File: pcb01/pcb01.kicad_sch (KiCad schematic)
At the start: 51 parts, among them J1 DIN41612_02x32_AC, J10 Conn_01x02_Socket, J11 Conn_01x09, J4 Display, J5 UART, J6 UART_IRQ, J7 Jmp_Irq, J8 Jmp_NMI, J9 Ram1 Enable, SW1 SW_Push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

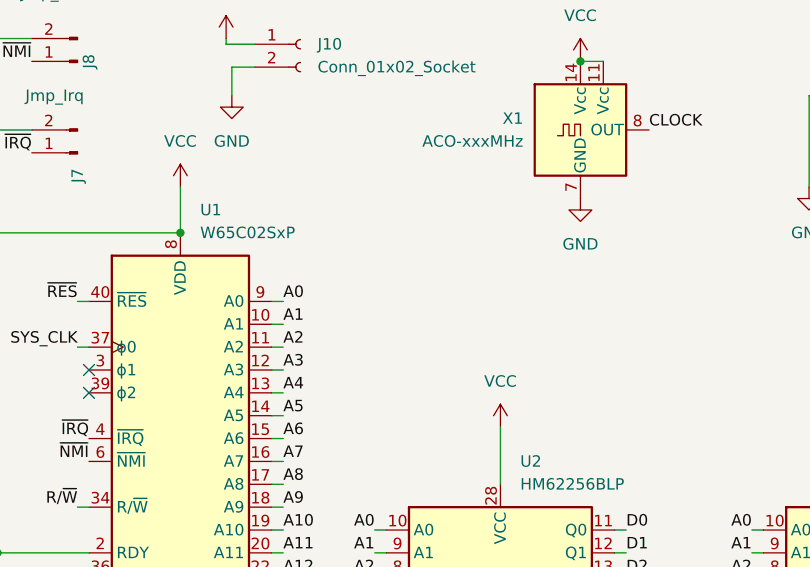
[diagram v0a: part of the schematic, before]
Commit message: fixed errors of first pcb (hopefully didn't mess up everything)
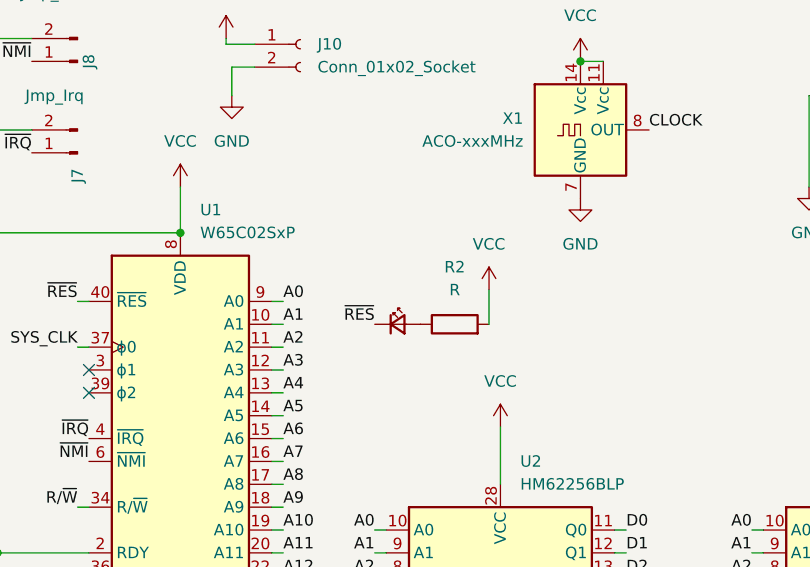
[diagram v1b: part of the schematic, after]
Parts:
- added D13: LED_Small, LED_SMD:LED_0805_2012Metric_Pad1.15x1.40mm_HandSolder, symbol Device:LED_Small
- added R2: R, Resistor_THT:R_Axial_DIN0207_L6.3mm_D2.5mm_P7.62mm_Horizontal, symbol Device:R
- C12, C13: footprint Capacitor_THT:CP_Radial_D5.0mm_P2.50mm -> Capacitor_THT:CP_Radial_D4.0mm_P2.00mm
- J6, J7, J8: footprint Connector_PinHeader_2.00mm:PinHeader_1x02_P2.00mm_Vertical -> Connector_PinSocket_2.54mm:PinSocket_1x02_P2.54mm_Vertical
- RN1, RN2, RN3: footprint Resistor_SMD:R_Array_Concave_4x0402 -> Resistor_SMD:R_Array_Convex_4x0612
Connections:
- net VCC: now also R2.2
- net ~{RES}: now also D13.1 (K)
- new net: D13.2 (A), R2.1
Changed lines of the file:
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@@
     (stroke (width 0) (type default))
   )
+  (wire (pts (xy 74.93 46.99) (xy 74.93 50.8))
+    (stroke (width 0) (type default))
+  )
   (wire (pts (xy 208.28 55.88) (xy 208.28 62.23))
     (stroke (width 0) (type default))
@@
     (effects (font (size 1.27 1.27)) (justify right bottom))
   )
+  (label "~{RES}" (at 62.23 50.8 180) (fields_autoplaced)
+    (effects (font (size 1.27 1.27)) (justify right bottom))
+  )
   (label "D3" (at 132.08 81.28 0) (fields_autoplaced)
     (effects (font (size 1.27 1.27)) (justify left bottom))
@@
       (effects (font (size 1.27 1.27)))
     )
-    (property "Footprint" "Connector_PinHeader_2.00mm:PinHeader_1x02_P2.00mm_Vertical" (at 29.21 31.75 0)
+    (property "Footprint" "Connector_PinSocket_2.54mm:PinSocket_1x02_P2.54mm_Vertical" (at 29.21 31.75 0)
       (effects (font (size 1.27 1.27)) hide)
     )
@@
     )
   )
+  (symbol (lib_id "Device:R") (at 71.12 50.8 90) (unit 1)
+    (in_bom yes) (on_board yes) (dnp no) (fields_autoplaced)
+    (property "Reference" "R2" (at 71.12 44.45 90)
+      (effects (font (size 1.27 1.27)))
+    )
+    (property "Value" "R" (at 71.12 46.99 90)
+      (effects (font (size 1.27 1.27)))
+    )
+    (property "Footprint" "Resistor_THT:R_Axial_DIN0207_L6.3mm_D2.5mm_P7.62mm_Horizontal" (at 71.12 52.578 90)
+      (effects (font (size 1.27 1.27)) hide)
+    )
+    (property "Datasheet" "~" (at 71.12 50.8 0)
+      (effects (font (size 1.27 1.27)) hide)
+    )
+    (pin "1")
+    (pin "2")
+    (instances
+      (project "pcb01"
+        (path "/a9a73dc6-7f92-4458-9da8-49621d12e480"
+          (reference "R2") (unit 1)
+        )
+      )
+    )
+  )
   (symbol (lib_id "Device:LED_Small") (at 279.4 143.51 0) (unit 1)
     (in_bom yes) (on_board yes) (dnp no)
@@
       (effects (font (size 1.27 1.27)))
     )
-    (property "Footprint" "Connector_PinHeader_2.00mm:PinHeader_1x02_P2.00mm_Vertical" (at 189.23 86.36 0)
+    (property "Footprint" "Connector_PinSocket_2.54mm:PinSocket_1x02_P2.54mm_Vertical" (at 189.23 86.36 0)
       (effects (font (size 1.27 1.27)) hide)
     )
@@
       (effects (font (size 1.27 1.27)))
     )
-    (property "Footprint" "Connector_PinHeader_2.00mm:PinHeader_1x02_P2.00mm_Vertical" (at 29.21 21.59 0)
+    (property "Footprint" "Connector_PinSocket_2.54mm:PinSocket_1x02_P2.54mm_Vertical" (at 29.21 21.59 0)
       (effects (font (size 1.27 1.27)) hide)
     )
@@
       (effects (font (size 1.27 1.27)) hide)
     )
-    (property "Footprint" "Resistor_SMD:R_Array_Concave_4x0402" (at 267.97 92.075 90)
+    (property "Footprint" "Resistor_SMD:R_Array_Convex_4x0612" (at 267.97 92.075 90)
       (effects (font (size 1.27 1.27)) hide)
     )
@@
       (effects (font (size 1.27 1.27)) (justify left))
     )
-    (property "Footprint" "Capacitor_THT:CP_Radial_D5.0mm_P2.50mm" (at 260.6802 24.765 0)
+    (property "Footprint" "Capacitor_THT:CP_Radial_D4.0mm_P2.00mm" (at 260.6802 24.765 0)
       (effects (font (size 1.27 1.27)) hide)
     )
@@
       (effects (font (size 1.27 1.27)) hide)
     )
-    (property "Footprint" "Resistor_SMD:R_Array_Concave_4x0402" (at 271.78 131.445 90)
+    (property "Footprint" "Resistor_SMD:R_Array_Convex_4x0612" (at 271.78 131.445 90)
       (effects (font (size 1.27 1.27)) hide)
     )
@@
     )
   )
+  (symbol (lib_id "power:VCC") (at 74.93 46.99 0) (unit 1)
+    (in_bom yes) (on_board yes) (dnp no) (fields_autoplaced)
+    (property "Reference" "#PWR037" (at 74.93 50.8 0)
+      (effects (font (size 1.27 1.27)) hide)
+    )
+    (property "Value" "VCC" (at 74.93 41.91 0)
+      (effects (font (size 1.27 1.27)))
+    )
+    (property "Footprint" "" (at 74.93 46.99 0)
+      (effects (font (size 1.27 1.27)) hide)
+    )
+    (property "Datasheet" "" (at 74.93 46.99 0)
+      (effects (font (size 1.27 1.27)) hide)
+    )
+    (pin "1")
+    (instances
+      (project "pcb01"
+        (path "/a9a73dc6-7f92-4458-9da8-49621d12e480"
+          (reference "#PWR037") (unit 1)
+        )
+      )
+    )
+  )
   (symbol (lib_id "Connector:Conn_01x02_Socket") (at 53.975 19.685 0) (unit 1)
     (in_bom yes) (on_board yes) (dnp no) (fields_autoplaced)
@@
       (effects (font (size 1.27 1.27)) (justify left))
     )
-    (property "Footprint" "Capacitor_THT:CP_Radial_D5.0mm_P2.50mm" (at 254.9652 24.765 0)
+    (property "Footprint" "Capacitor_THT:CP_Radial_D4.0mm_P2.00mm" (at 254.9652 24.765 0)
       (effects (font (size 1.27 1.27)) hide)
     )
@@
       (effects (font (size 1.27 1.27)) hide)
     )
-    (property "Footprint" "Resistor_SMD:R_Array_Concave_4x0402" (at 267.97 80.645 90)
+    (property "Footprint" "Resistor_SMD:R_Array_Convex_4x0612" (at 267.97 80.645 90)
       (effects (font (size 1.27 1.27)) hide)
     )
@@
         )
       )
+    )
+  )
+  (symbol (lib_id "Device:LED_Small") (at 64.77 50.8 0) (unit 1)
+    (in_bom yes) (on_board yes) (dnp no)
+    (property "Reference" "D13" (at 69.85 50.8 0)
+      (effects (font (size 1.27 1.27)) hide)
+    )
+    (property "Value" "LED_Small" (at 64.8335 46.99 0)
+      (effects (font (size 1.27 1.27)) hide)
+    )
+    (property "Footprint" "LED_SMD:LED_0805_2012Metric_Pad1.15x1.40mm_HandSolder" (at 64.77 50.8 90)
+      (effects (font (size 1.27 1.27)) hide)
+    )
+    (property "Datasheet" "~" (at 64.77 50.8 90)
+      (effects (font (size 1.27 1.27)) hide)
+    )
+    (pin "1")
+    (pin "2")
+    (instances
+      (project "pcb01"
+        (path "/a9a73dc6-7f92-4458-9da8-49621d12e480"
+          (reference "D13") (unit 1)
+        )
+      )

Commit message: big chunk of new pcb done
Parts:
- removed J4: Display, Connector_PinSocket_2.54mm:PinSocket_1x16_P2.54mm_Vertical, symbol Connector:Conn_01x16_Socket
- removed J6: UART_IRQ, Connector_PinSocket_2.54mm:PinSocket_1x02_P2.54mm_Vertical, symbol Connector:Conn_01x02_Socket
- removed RV1: R_LCD_BIAS, Potentiometer_THT:Potentiometer_Vishay_T73YP_Vertical, symbol Device:R_Potentiometer_Small
- removed U8: R565c52, Package_DIP:DIP-40_W15.24mm_Socket, symbol 65xx:R565c52
- added C14: C, Capacitor_THT:C_Disc_D4.7mm_W2.5mm_P5.00mm, symbol Device:C
- added U10: TL28L92FR, Package_QFP:MQFP-44_10x10mm_P0.8mm, symbol 2024-09-25_17-04-06:TL28L92FR
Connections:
- net A0: now also J1.a17 (Pin_a17), U10.40 (A0); no longer J1.c31 (Pin_c31)
- net A1: now also J1.a16 (Pin_a16), U10.42 (A1); no longer J1.c30 (Pin_c30)
- net A10: now also J1.a7 (Pin_a7); no longer J1.c21 (Pin_c21)
- net A11: now also J1.a6 (Pin_a6); no longer J1.c20 (Pin_c20)
- net A12: now also J1.a5 (Pin_a5); no longer J1.c19 (Pin_c19)
- net A13: now also J1.a4 (Pin_a4); no longer J1.c18 (Pin_c18)
- net A14: now also J1.a3 (Pin_a3); no longer J1.c17 (Pin_c17)
- net A15: now also J1.a2 (Pin_a2); no longer J1.c16 (Pin_c16)
- net A2: now also J1.a15 (Pin_a15), U10.44 (A2); no longer J1.c29 (Pin_c29)
- net A3: now also J1.a14 (Pin_a14), U10.1 (A3); no longer J1.c28 (Pin_c28)
- net A4: now also J1.a13 (Pin_a13); no longer J1.c27 (Pin_c27)
- net A5: now also J1.a12 (Pin_a12); no longer J1.c26 (Pin_c26)
- net A6: now also J1.a11 (Pin_a11); no longer J1.c25 (Pin_c25)
- net A7: now also J1.a10 (Pin_a10); no longer J1.c24 (Pin_c24)
- net A8: now also J1.a9 (Pin_a9); no longer J1.c23 (Pin_c23)
- net A9: now also J1.a8 (Pin_a8); no longer J1.c22 (Pin_c22)
- net D0: now also U10.22 (D0)
- net D1: now also U10.12 (D1)
- net D2: now also U10.21 (D2)
- net D3: now also U10.13 (D3)
- net D4: now also U10.20 (D4)
- net D5: now also U10.14 (D5)
- net D6: now also U10.19 (D6)
- net D7: now also U10.15 (D7)
- net GND: now also J1.c18 (Pin_c18), C14.2, U10.16 (GND), U10.17 (GND); no longer J1.c15 (Pin_c15)
- net RX_D1: now also U10.29 (RXDA)
- net RX_D2: now also U10.5 (RXDB)
- net SYS_CLK: now also J1.a22 (Pin_a22); no longer J1.a3 (Pin_a3)
- net TX_D1: now also U10.28 (TXDA)
- net TX_D2: now also U10.6 (TXDB)
- net UART_X1: now also U10.30 (X1/CLK)
- net UART_X2: now also U10.31 (X2)
- net VCC: now also J1.a18 (Pin_a18), C14.1, U10.11 (I/M), U10.38 (VCC), U10.39 (VCC); no longer J1.a15 (Pin_a15)
- net ~{IOEN_00_GPIO0}: now also J1.a24 (Pin_a24); no longer J1.a31 (Pin_a31)
- net ~{IOEN_02_UART}: now also U10.33 (CEN)
- net ~{IOEN_03}: now also J1.a27 (Pin_a27); no longer J1.a28 (Pin_a28)
- net ~{IOEN_04}: now also J1.a28 (Pin_a28); no longer J1.a27 (Pin_a27)
- net ~{IOEN_05}: now also J1.a29 (Pin_a29); no longer J1.a26 (Pin_a26)
- net ~{IOEN_06}: now also J1.a30 (Pin_a30); no longer J1.a25 (Pin_a25)
- net ~{IOEN_07}: now also J1.a31 (Pin_a31); no longer J1.a24 (Pin_a24)
- net ~{QOE}: now also U10.4 (RDN); no longer J1.a5 (Pin_a5)
- net ~{QWE_RAM}: now also U10.3 (WRN); no longer J1.a4 (Pin_a4)
- net ~{RES}: no longer J1.a2 (Pin_a2)
- net ~{SYS_CLK}: now also J1.a21 (Pin_a21); no longer J1.a16 (Pin_a16)
- net RES: now reaches U9.5 (RST)
- net RES: now also U10.32 (RESET)
- net DISP_EN: no longer names the net of U4.21 (O2)
- net DISP_EN: no longer J1.a30 (Pin_a30)
- net ~{IOEN_01_DISP}: no longer names the net of U4.3 (I1)
- net ~{IOEN_01_DISP}: no longer U5.14 (O1)
- new net ~{IOEN_01}: J1.a25 (Pin_a25), U5.14 (O1)
- no-connect marks 37 -> 33
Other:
- moved on the sheet: C1, C10, C11, C12, C13, C2, C3, C4, C5, C6, C7, C8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

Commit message: more routing
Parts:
- added J2: Jmp_UART_Irq, Connector_PinSocket_2.54mm:PinSocket_1x02_P2.54mm_Vertical, symbol Connector:Conn_01x02_Pin
- added J3: Conn_01x09_Socket, Connector_PinHeader_2.54mm:PinHeader_1x09_P2.54mm_Vertical, symbol Connector:Conn_01x09_Socket
- added J4: Conn_01x08_Socket, Connector_PinSocket_2.54mm:PinSocket_1x08_P2.54mm_Vertical, symbol Connector:Conn_01x08_Socket
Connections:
- net GND: now also J3.1 (Pin_1), J4.1 (Pin_1)
- net UART_OP7: now reaches U10.10 (OP7)
- net UART_OP7: now also J3.9 (Pin_9)
- net ~{IRQ_UART}: now reaches U10.18 (INTRN)
- net ~{IRQ_UART}: now also J2.2 (Pin_2)
- net UART_IP0: now reaches U10.2 (IP0)
- net UART_IP0: now also J4.2 (Pin_2)
- net UART_OP6: now reaches U10.24 (OP6)
- net UART_OP6: now also J3.8 (Pin_8)
- net UART_OP4: now reaches U10.25 (OP4)
- net UART_OP4: now also J3.6 (Pin_6)
- net UART_OP2: now reaches U10.26 (OP2)
- net UART_OP2: now also J3.4 (Pin_4)
- net UART_OP0: now reaches U10.27 (OP0)
- net UART_OP0: now also J3.2 (Pin_2)
- net UART_IP2: now reaches U10.34 (IP2)
- net UART_IP2: now also J4.4 (Pin_4)
- net UART_IP6: now reaches U10.35 (IP6)
- net UART_IP6: now also J4.8 (Pin_8)
- net UART_IP5: now reaches U10.36 (IP5)
- net UART_IP5: now also J4.7 (Pin_7)
- net UART_IP4: now reaches U10.37 (IP4)
- net UART_IP4: now also J4.6 (Pin_6)
- net UART_IP3: now reaches U10.41 (IP3)
- net UART_IP3: now also J4.5 (Pin_5)
- net UART_IP1: now reaches U10.43 (IP1)
- net UART_IP1: now also J4.3 (Pin_3)
- net UART_OP1: now reaches U10.7 (OP1)
- net UART_OP1: now also J3.3 (Pin_3)
- net UART_OP3: now reaches U10.8 (OP3)
- net UART_OP3: now also J3.5 (Pin_5)
- net UART_OP5: now reaches U10.9 (OP5)
- net UART_OP5: now also J3.7 (Pin_7)
- no-connect marks 33 -> 18

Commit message: finished mark2 pcb kind of
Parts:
- added R3: R, Resistor_THT:R_Axial_DIN0207_L6.3mm_D2.5mm_P7.62mm_Horizontal, symbol Device:R
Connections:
- net GND: now also J2.1 (Pin_1)
- net GPIO00_O0: now also D1.2 (A); no longer D4.2 (A)
- net GPIO00_O1: now also D2.2 (A); no longer D3.2 (A)
- net GPIO00_O2: now also D3.2 (A); no longer D2.2 (A)
- net GPIO00_O3: now also D4.2 (A); no longer D1.2 (A)
- net GPIO00_O4: now also D5.2 (A); no longer D8.2 (A)
- net GPIO00_O5: now also D6.2 (A); no longer D7.2 (A)
- net GPIO00_O6: now also D7.2 (A); no longer D6.2 (A)
- net GPIO00_O7: now also D8.2 (A); no longer D5.2 (A)
- net VCC: now also R3.1
- net ~{IRQ_UART}: now also R3.2
- net at D4.1 (K): now also RN1.4 (R4.1); no longer RN1.1 (R1.1)
- net at D6.1 (K): now also RN2.2 (R2.1); no longer RN2.3 (R3.1)
- net at RN1.3 (R3.1): now also D3.1 (K); no longer D2.1 (K)
- net at D8.1 (K): now also RN2.4 (R4.1); no longer RN2.1 (R1.1)
- net at D7.1 (K): now also RN2.3 (R3.1); no longer RN2.2 (R2.1)
- net at D5.1 (K): now also RN2.1 (R1.1); no longer RN2.4 (R4.1)
- net at RN1.2 (R2.1): now also D2.1 (K); no longer D3.1 (K)
- net at D1.1 (K): now also RN1.1 (R1.1); no longer RN1.4 (R4.1)
- no-connect marks 18 -> 17

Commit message: add power switch etc
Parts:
- removed J10: Conn_01x02_Socket, Connector_PinSocket_2.54mm:PinSocket_1x02_P2.54mm_Vertical, symbol Connector:Conn_01x02_Socket
- added J6: Conn_01x02_Socket, Connector_PinSocket_2.54mm:PinSocket_1x02_P2.54mm_Vertical, symbol Connector:Conn_01x02_Socket
- added SW2: SW_DPDT_x2, sim82:7x7DPDT, symbol Switch:SW_DPDT_x2
- J3: footprint Connector_PinHeader_2.54mm:PinHeader_1x09_P2.54mm_Vertical -> Connector_PinSocket_2.54mm:PinSocket_1x09_P2.54mm_Vertical
- J7, J8: footprint Connector_PinSocket_2.54mm:PinSocket_1x02_P2.54mm_Vertical -> Connector_PinHeader_2.54mm:PinHeader_1x02_P2.54mm_Vertical
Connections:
- net GND: now also SW2.4 (A)
- net VCC: now also R3.2, SW2.1 (A); no longer R3.1
- net ~{IRQ_UART}: now also R3.1; no longer R3.2
- new net: J6.1 (Pin_1), SW2.2 (B)
- new net: J6.2 (Pin_2), SW2.5 (B)
- no-connect marks 17 -> 19
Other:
- moved on the sheet: C1, C10, C11, C12, C13, C14, C2, C3, C4, C5, C6, C7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

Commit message: finalized (?) pcb
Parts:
- added H1, H2: GND, MountingHole:MountingHole_3.2mm_M3_DIN965_Pad, symbol Mechanical:MountingHole_Pad
- C3, C4: value C -> 100uF
- SW1: value SW_Push -> SW_Reset
- SW2: value SW_DPDT_x2 -> SW_PWR
- U2, U7: value HM62256BLP -> H3-65756H-5
- U4: value PAL20RS10 -> ATF22V10
- X1: value ACO-xxxMHz -> ACO-14MHz
- Y1: value Crystal -> Crystal 3.6864MHz
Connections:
- net GND: now also H1.1, H2.1; no longer RN3.5 (R4.2), RN3.6 (R3.2), RN3.7 (R2.2), RN3.8 (R1.2)
- net RES: now also J1.c30 (Pin_c30)
- net VCC: now also RN3.5 (R4.2), RN3.6 (R3.2), RN3.7 (R2.2), RN3.8 (R1.2)
- net ~{CS_RAM0}: now also D10.1 (K); no longer D10.2 (A)
- net ~{CS_RAM1}: now also D11.1 (K); no longer D11.2 (A)
- net ~{CS_ROM}: now also D9.1 (K); no longer D9.2 (A)
- net ~{QWE_RAM}: now also D12.1 (K); no longer D12.2 (A)
- net ~{RES}: now also J1.c31 (Pin_c31)
- net at RN3.2 (R2.1): now also D11.2 (A); no longer D11.1 (K)
- net at RN3.1 (R1.1): now also D12.2 (A); no longer D12.1 (K)
- net at RN3.3 (R3.1): now also D10.2 (A); no longer D10.1 (K)
- net at RN3.4 (R4.1): now also D9.2 (A); no longer D9.1 (K)
- no-connect marks 19 -> 35
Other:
- moved on the sheet: C10, C11, C12, C13, C14, C3, C4, C5, C6, C7, C8, C9
